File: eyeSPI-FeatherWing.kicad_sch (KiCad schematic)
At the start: 14 parts, among them SW1 KMR2, X1 EYE_SPI_DISPLAY_FLIP

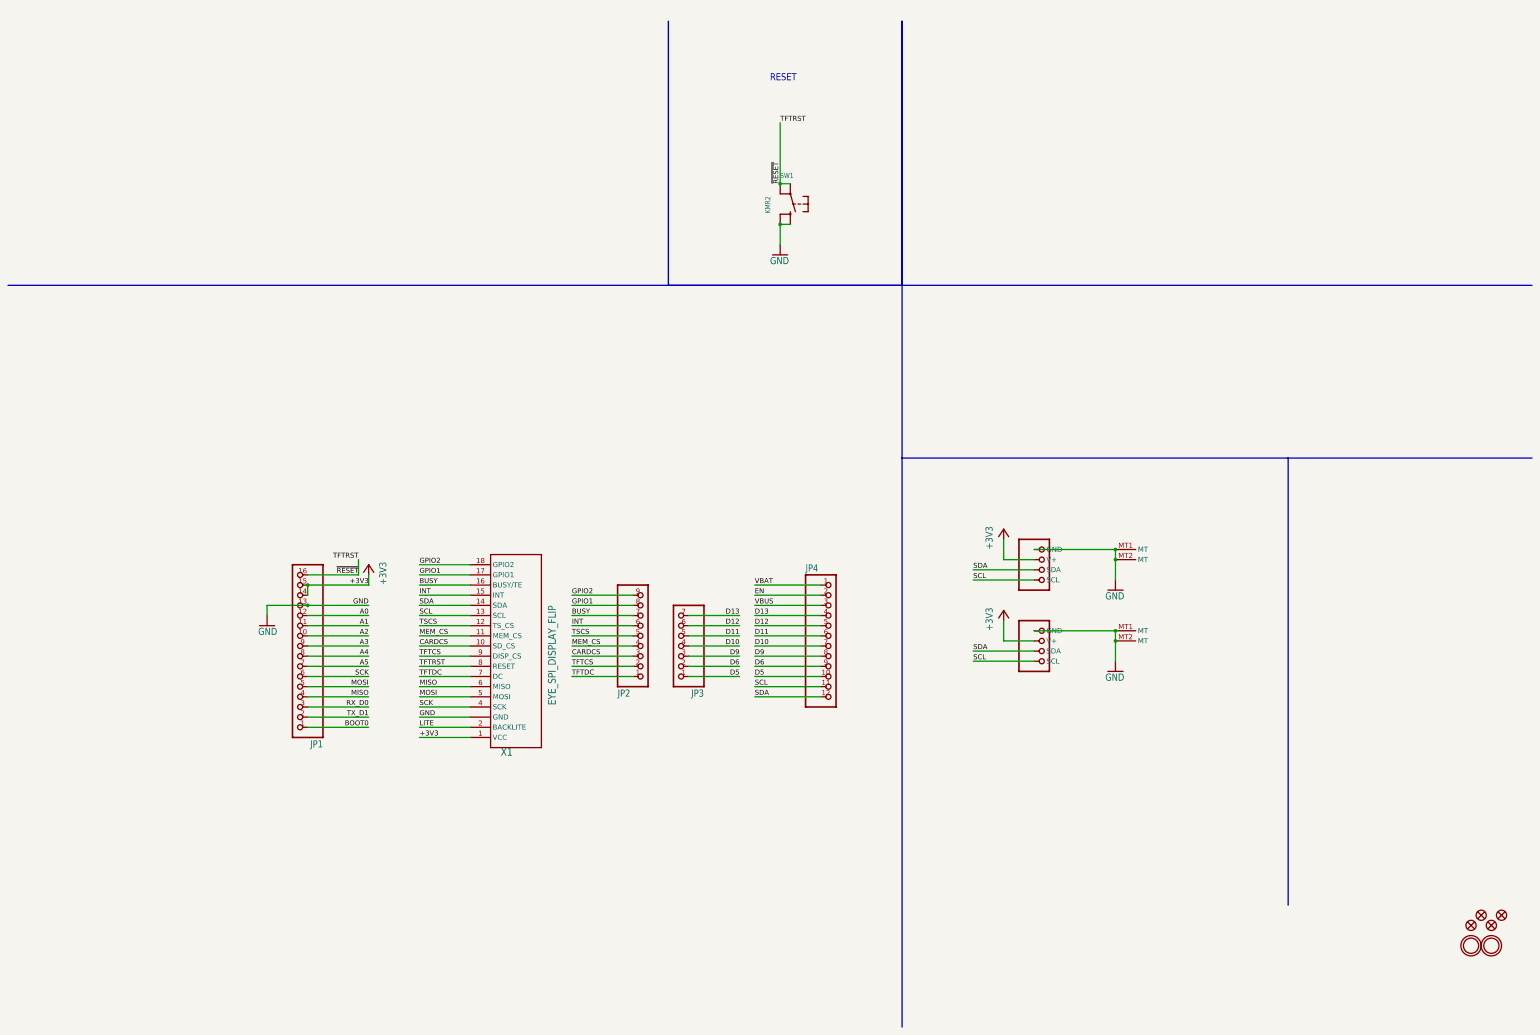
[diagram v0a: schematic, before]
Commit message: Cleanup Schematic; Add Footprints path to project.
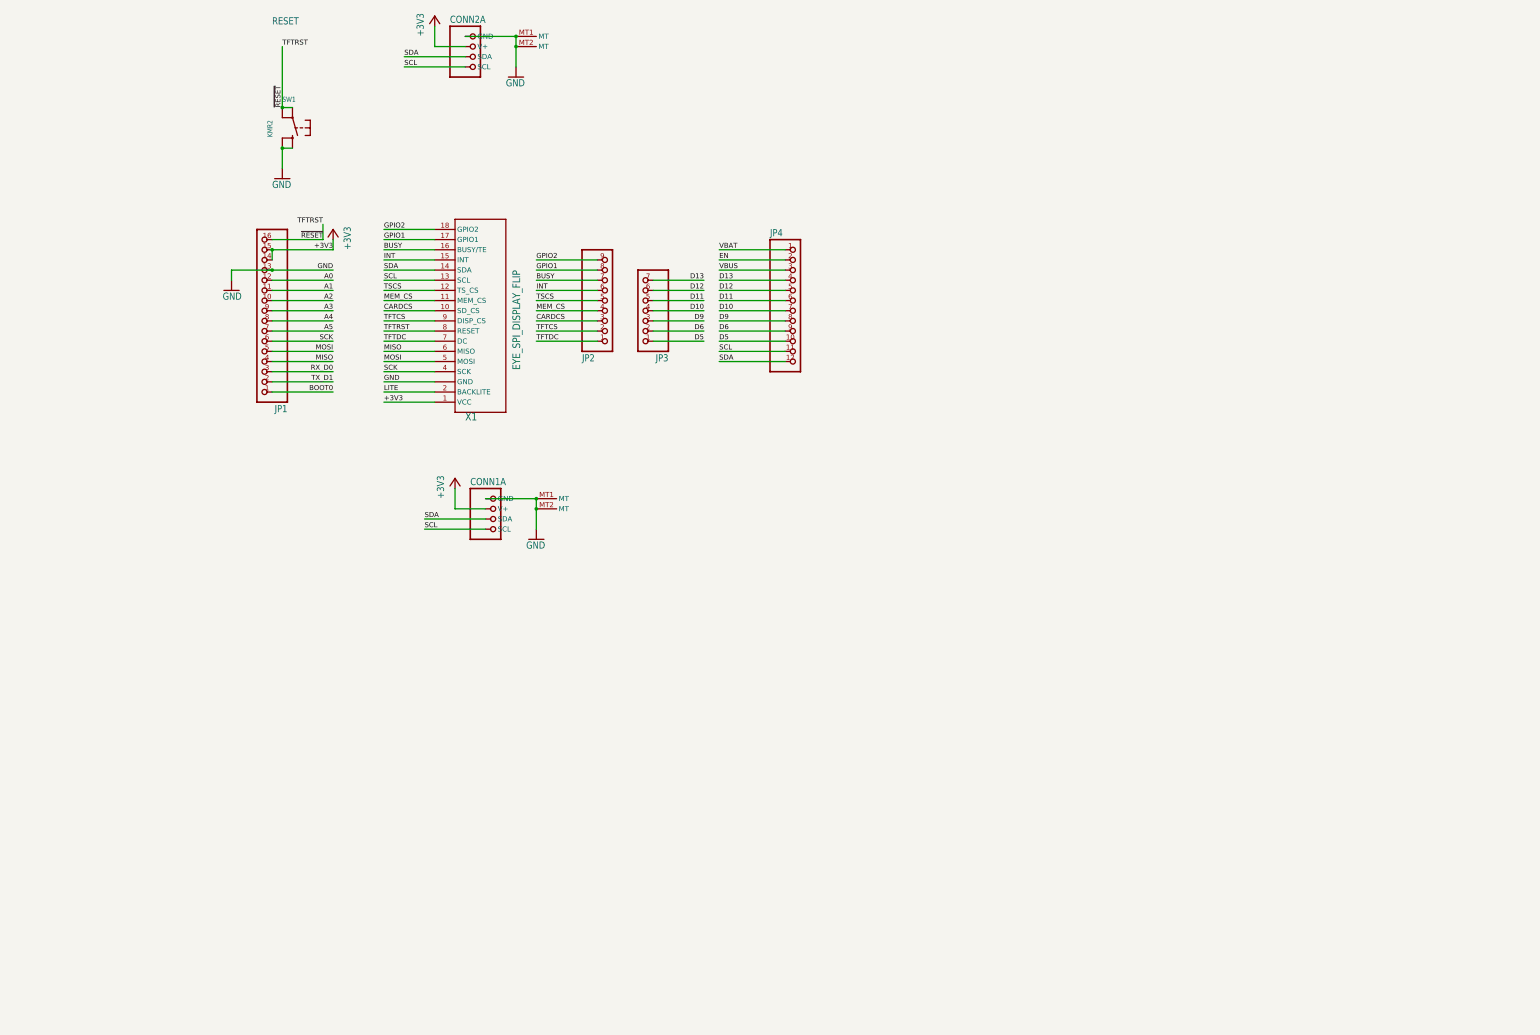
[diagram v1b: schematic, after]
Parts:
- removed U$31, U$32: MOUNTINGHOLE2.5, eyeSPI-FeatherWing:MOUNTINGHOLE_2.5_PLATED, symbol eyeSPI-FeatherWing-eagle-import:MOUNTINGHOLE2.5
- removed U$34, U$35, U$37, U$5: FIDUCIAL_1MM, eyeSPI-FeatherWing:FIDUCIAL_1MM, symbol eyeSPI-FeatherWing-eagle-import:FIDUCIAL_1MM
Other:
- title: (none) -> EyeSPI FeatherWing
- moved on the sheet: JP1, JP2, JP3, JP4, SW1, X1
